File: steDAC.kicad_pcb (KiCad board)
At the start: 2 copper layers, 100 x 80 mm, 148 parts, among them IC10 TPS7A3001DGNT, IC11 ADP150AUJZ-3.3-R7, IC2 ES9038Q2M, IC3 ATSAMS70N20A-AN, IC4 ADP150AUJZ-3.3-R7, IC5 ADP150AUJZ-3.3-R7, IC6 ADP150AUJZ-3.3-R7, IC7 ADP150AUJZ-3.3-R7, IC8 LT1026CS8#PBF, IC9 ADP7118ARDZ, J2 USB4105-GF-A, J3 Conn_02x05_Odd_Even, J5 Conn_01x02, J6 Conn_01x04, J7 STX-3120-5B-284C, U2 OPA1612-Q1, U3 OPA1612-Q1, U4 OPA1622, Y2 SiT8209AI-21-33S-100.000000X, Y3 12MHz

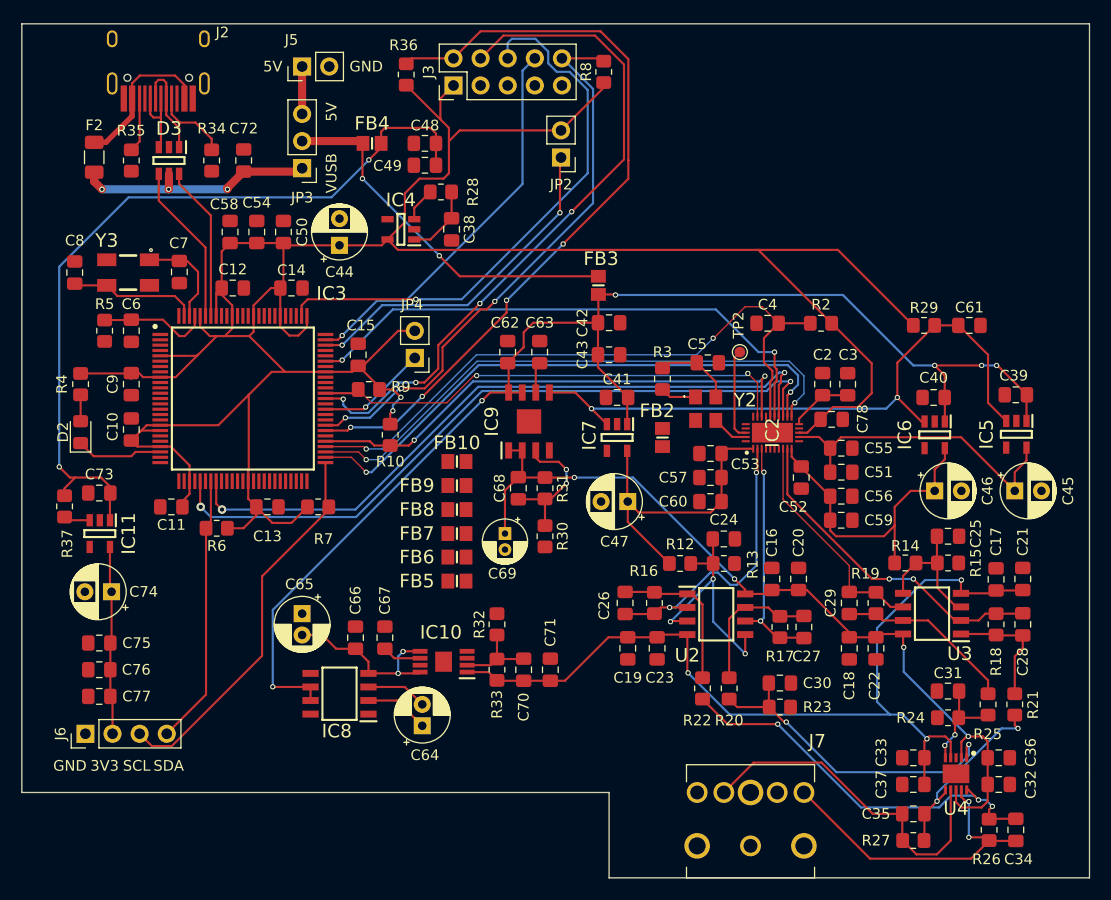
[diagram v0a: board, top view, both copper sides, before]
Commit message: Adding some missing nets
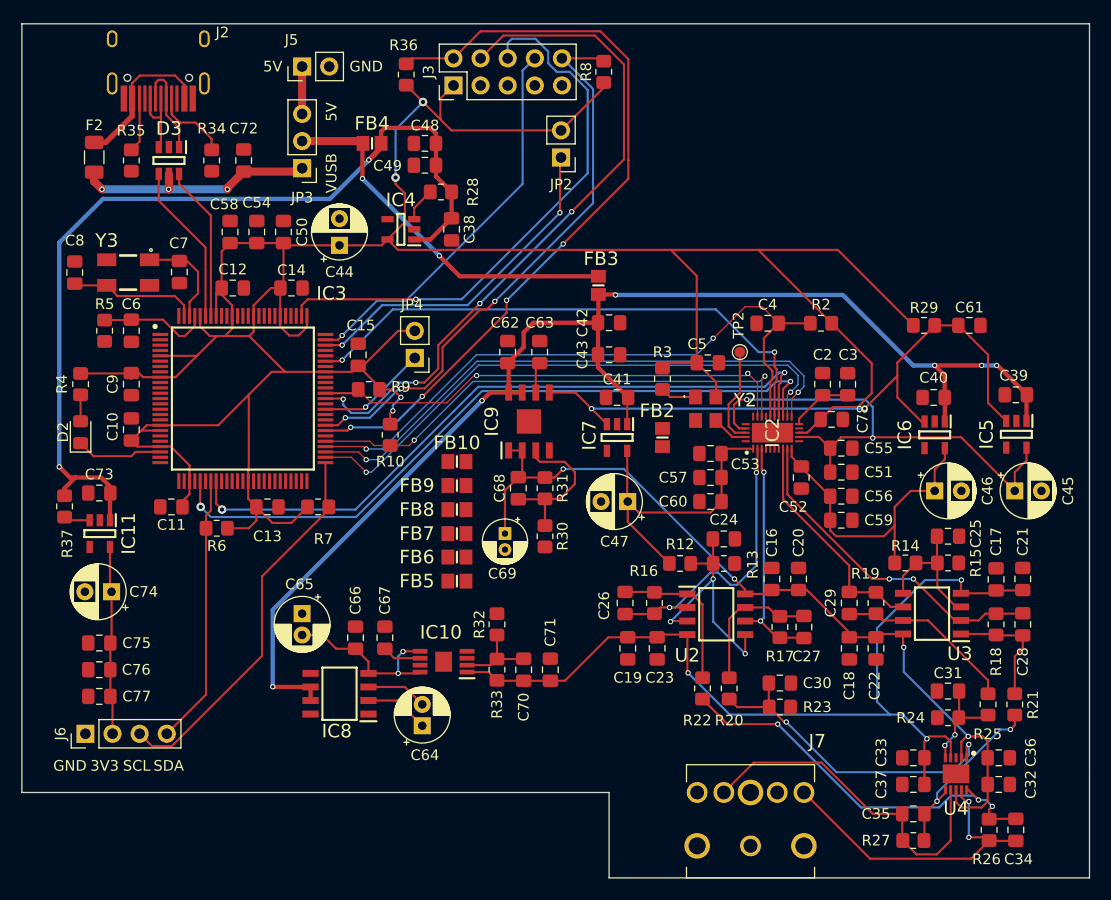
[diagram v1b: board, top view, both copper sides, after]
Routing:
- net +3.3VDAC: track 29.9 -> 49.4 mm, vias 0 -> 2
- net +3V3: track 274.2 -> 286.6 mm, vias 2 -> 4
- net MCU_5V: track 81.1 -> 85.5 mm
- net Net-(C68-Pad1): track 12.9 -> 14.4 mm, vias 2 -> 0
- net DAC_PWR_EN: track 60.4 -> 61.3 mm
- net +VDAC: track 79.6 -> 80.2 mm
- net Net-(IC2-Pad28): track 8.59 -> 9.23 mm
- net Net-(C35-Pad1): track 18.4 -> 17.8 mm

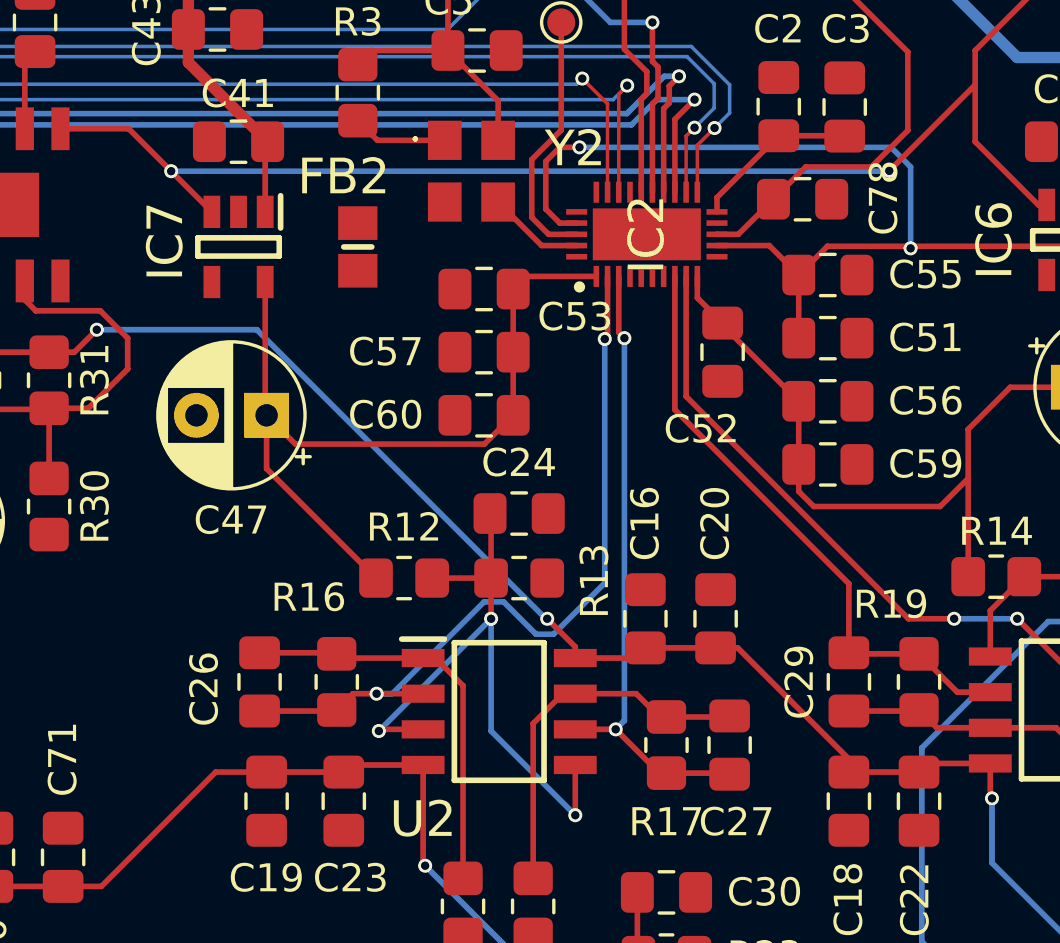
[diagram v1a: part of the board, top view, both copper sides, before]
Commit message: Moving some traces around
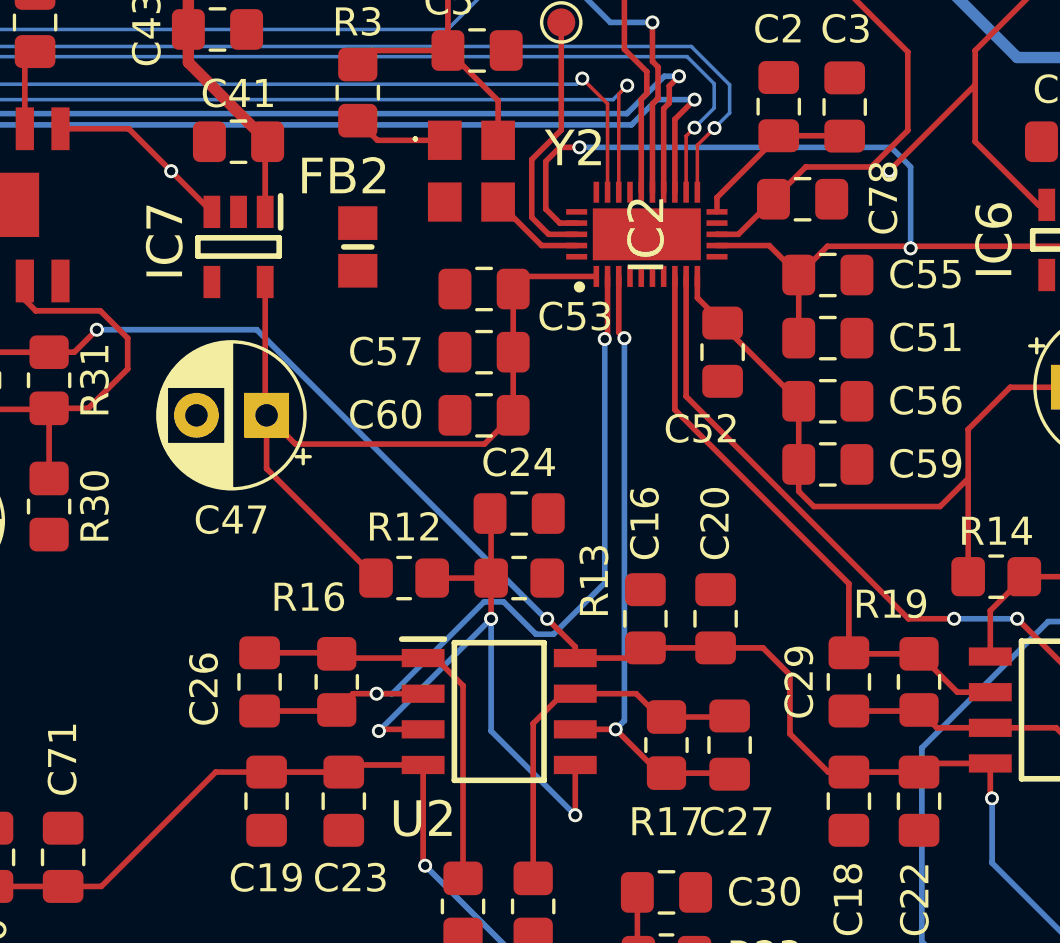
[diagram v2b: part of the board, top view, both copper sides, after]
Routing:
- net DAC_PWR_EN: track 61.3 -> 35.7 mm
- net +VDAC: track 80.2 -> 81.2 mm
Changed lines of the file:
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@@
   (segment (start 240.4625 141.25) (end 240.4625 138.75) (width 0.2032) (layer "F.Cu") (net 9))
   (segment (start 199 112.5) (end 196.5375 112.5) (width 0.2032) (layer "F.Cu") (net 9))
-  (segment (start 227.5 127) (end 227.5 127.4625) (width 0.2032) (layer "F.Cu") (net 9))
   (segment (start 230.3075 127.155) (end 232.539 127.155) (width 0.2032) (layer "F.Cu") (net 9))
   (segment (start 239.9 143.4) (end 240.4625 142.8375) (width 0.2032) (layer "F.Cu") (net 9))
@@
   (segment (start 238 137.25) (end 238 138.75) (width 0.2032) (layer "F.Cu") (net 9))
   (segment (start 220.25 123.0375) (end 219.8875 123.4) (width 0.2032) (layer "F.Cu") (net 9))
+  (segment (start 226.7625 127.4625) (end 227.5 127.4625) (width 0.2032) (layer "F.Cu") (net 9))
   (segment (start 240 136.75) (end 238.65 136.75) (width 0.2032) (layer "F.Cu") (net 9))
   (segment (start 237.5 142.9) (end 238 143.4) (width 0.2032) (layer "F.Cu") (net 9))
   (segment (start 240.4625 142.8375) (end 240.4625 141.25) (width 0.2032) (layer "F.Cu") (net 9))
-  (segment (start 223.5375 123.0375) (end 227.5 127) (width 0.2032) (layer "F.Cu") (net 9))
   (segment (start 196.5 112.4625) (end 195.25 113.7125) (width 0.2032) (layer "F.Cu") (net 9))
   (segment (start 238.65 136.75) (end 238.5 136.75) (width 0.2032) (layer "F.Cu") (net 9))
@@
   (segment (start 195.25 113.7125) (end 195.25 117.75) (width 0.2032) (layer "F.Cu") (net 9))
   (segment (start 237.5 141.75) (end 237.5 142.9) (width 0.2032) (layer "F.Cu") (net 9))
-  (segment (start 222.75 123.0375) (end 223.5375 123.0375) (width 0.2032) (layer "F.Cu") (net 9))
+  (segment (start 225.4 126.1) (end 226.7625 127.4625) (width 0.2032) (layer "F.Cu") (net 9))
   (segment (start 219.8875 123.4) (end 217.75 123.4) (width 0.2032) (layer "F.Cu") (net 9))
   (segment (start 232.539 128.339) (end 232.6 128.4) (width 0.2032) (layer "F.Cu") (net 9))
+  (segment (start 225.4 124) (end 225.4 126.1) (width 0.2032) (layer "F.Cu") (net 9))
   (segment (start 196.865 109.962) (end 195.595 109.962) (width 0.2032) (layer "F.Cu") (net 9))
   (segment (start 196.865 112.0975) (end 196.865 109.962) (width 0.2032) (layer "F.Cu") (net 9))
+  (segment (start 224.4375 123.0375) (end 225.4 124) (width 0.2032) (layer "F.Cu") (net 9))
   (segment (start 220.25 123.0375) (end 222.75 123.0375) (width 0.2032) (layer "F.Cu") (net 9))
   (segment (start 240.4625 138.75) (end 240.4625 137.2125) (width 0.2032) (layer "F.Cu") (net 9))
+  (segment (start 222.75 123.0375) (end 224.4375 123.0375) (width 0.2032) (layer "F.Cu") (net 9))
   (segment (start 230 127.4625) (end 230.3075 127.155) (width 0.2032) (layer "F.Cu") (net 9))
   (segment (start 232.539 127.155) (end 232.539 128.339) (width 0.2032) (layer "F.Cu") (net 9))
@@
   (via (at 203.35 106.05) (size 0.5) (drill 0.3) (layers "F.Cu" "B.Cu") (net 30))
   (segment (start 228.938556 106.038556) (end 228.927112 106.05) (width 0.2) (layer "B.Cu") (net 30))
-  (segment (start 228.927112 106.05) (end 203.35 106.05) (width 0.2) (layer "B.Cu") (net 30))
   (segment (start 198.135 102.1525) (end 198.5 101.7875) (width 0.2032) (layer "F.Cu") (net 31))
   (segment (start 198.135 104.538) (end 198.135 102.1525) (width 0.2032) (layer "F.Cu") (net 31))
